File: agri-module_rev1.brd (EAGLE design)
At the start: 44 x 40 mm, 39 parts, among them M1 DMG1023, U2 PCA9570, U3 APDS-9960

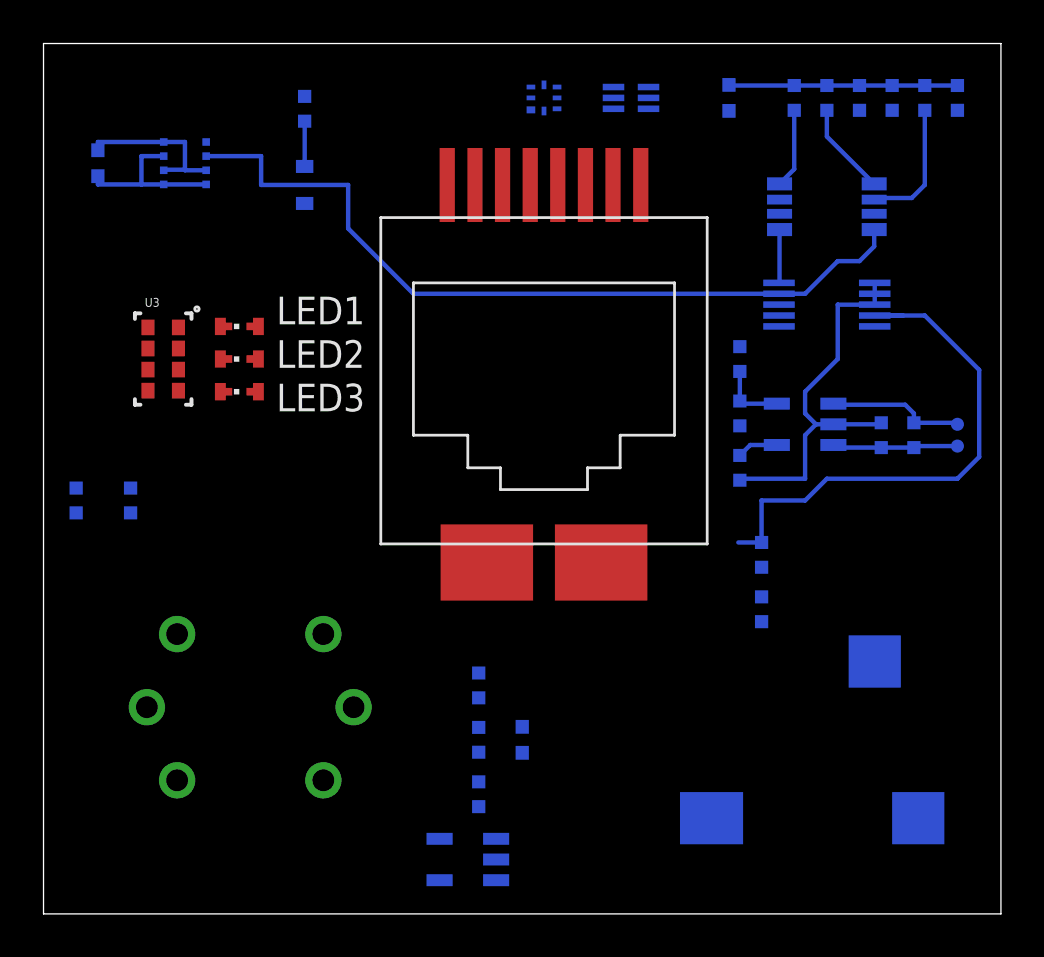
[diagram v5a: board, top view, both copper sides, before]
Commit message: Audit 1 w/ notes (wired / ready for feedback...)
______________________________________________
Schematic Feedback:
______________________________________________|
-no "zero length" junctions to parts
-add more labels, less long/jumbled connections
-tighten up the look
-replace 5v Power FET with higher power part (6601 or SIA5)
>(These are Dual N+P fets, use as darlington. Inverts signal back
aswell...)
-add very weak pull-up/downs to any fet gates. These should never be
floating
-copy michaels de-coupl caps to apds-9960
-add atleast 0R's to everything, so you dont need to cut traces
-add "lvl-trans/isolation-filter" FETs (poor mans) to i2c lines (check
Michaels schema...)
-***change i2c switch Vcc to 3.6v_HP! (otherwise, can't talk to further
boards if off)
-add RC to any power switches, so you don't get "inrush oscillation"
-add de-coupling caps and resistors to Vcc line PER PART

______________________________________________
Layout Feedback:
______________________________________________|
-add i2c addresses to board silkscreen (helps dev)
-Add mills around parts for Thermo Isolation
-tighten width of polygone pours to match trace widths (0.2032)
-Can make vias smaller (down to 0.2!)

-Use Michael's AUX jack? Or stick with mine?

______________________________________________
Feature Changes to add/design:
______________________________________________|
-See if board can be standalone and run on 5v.
>Check if all parts can use 5v & add DIP switch.
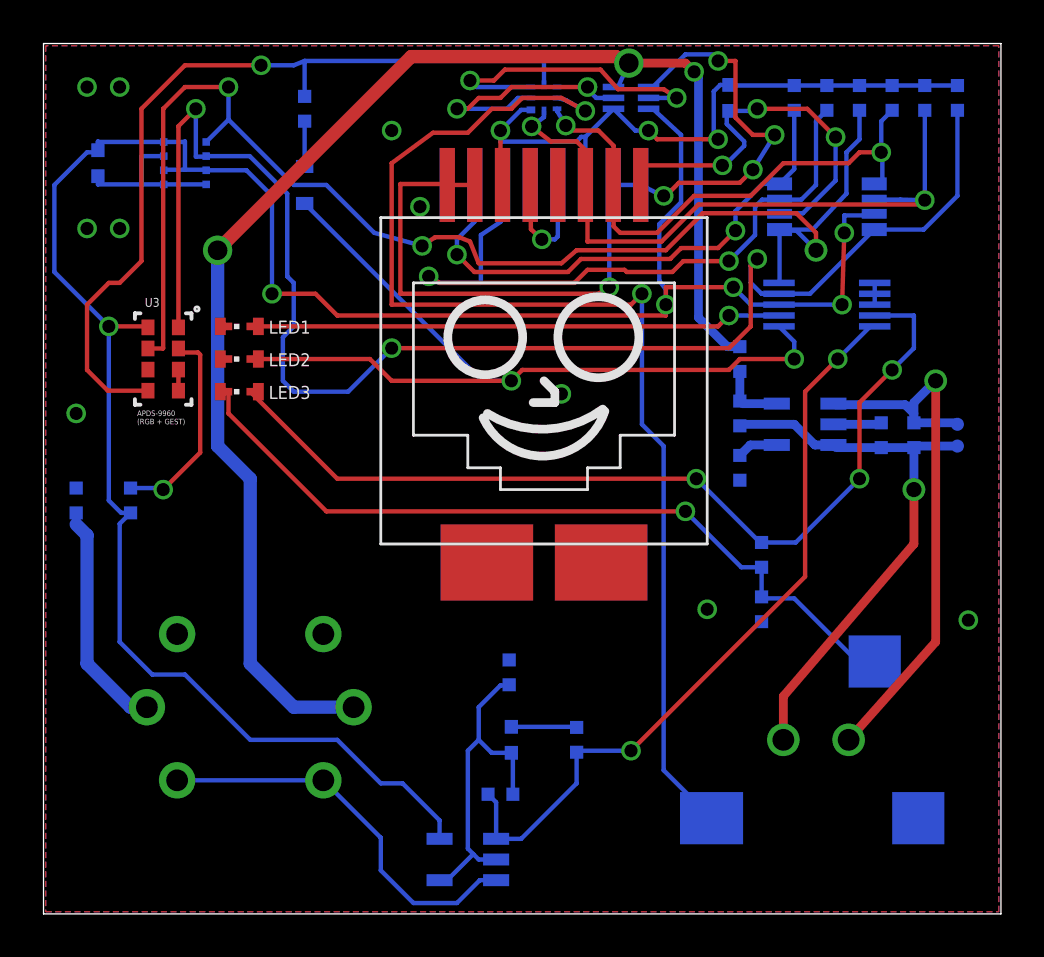
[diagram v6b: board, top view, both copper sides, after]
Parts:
- added U$9: RJ45_RA_SMD, BrainGrid - Electromechanical:RJ45_RA_SMD
- moved R18 6.00 mm to (36.0, 37.5)
- moved R3 4.50 mm to (42.0, 37.5)
- moved R7 4.50 mm to (24.5, 8.00), turned to 270 degrees
- moved R5 3.00 mm to (39.0, 37.5)
- moved R11 1.52 mm to (21.4, 11.1)
- moved R2 1.50 mm to (37.5, 37.5)
- moved R8 1.00 mm to (21.0, 5.50), turned to 0 degrees
- moved C3 0.50 mm to (21.5, 8.00), turned to 270 degrees
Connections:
- net 3.6V_HP: now also U$9.3; no longer U$5.5
- net 5V: now also U$9.1, U$9.2
- net GND: now also U$1.5, U$1.NC1, U$1.NC2, U$9.5, U$9.8, U$9.NC1, U$9.NC2; no longer U$1.7
- net N$14: now also U$1.6; no longer U$1.4
- net N$15: now also U$1.7; no longer U$1.6
- net N$7: now also U$9.6
- net N$8: now also U$9.7
- net T_SENSE: now also U$1.4, U$9.4; no longer U$1.5
- net VCC: now also U$5.5
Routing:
- net VCC: track 7.65 -> 106.5 mm, vias 0 -> 6
- net CO2_POW: track 0.00 -> 66.4 mm, vias 0 -> 3
- net N$3: track 2.46 -> 62.7 mm, vias 0 -> 3
- net EC_POW: track 0.00 -> 55.3 mm, vias 0 -> 2
- net 5V: track 0.00 -> 41.5 mm, vias 0 -> 5
- net LED_INDICATE: track 0.00 -> 40.5 mm, vias 0 -> 2
- net GEST_LED: track 0.00 -> 38.6 mm, vias 0 -> 1
- net EC_SENSE: track 0.00 -> 36.2 mm, vias 0 -> 1
- net N$16: track 0.00 -> 35.2 mm, vias 0 -> 2
- net N$11: track 36.9 -> 69.3 mm, vias 0 -> 3
- net N$7: track 0.00 -> 31.9 mm, vias 0 -> 2
- net N$14: track 6.03 -> 33.3 mm, vias 0 -> 2
- net N$5: track 0.00 -> 24.5 mm, vias 0 -> 1
- net 3.6V_HP: track 10.5 -> 31.9 mm, vias 0 -> 3
- net N$15: track 4.28 -> 25.5 mm, vias 0 -> 2
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- added copper zone on layer 1, net GND
- added copper zone on layer 16, net GND
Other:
- board text added: "( )"
- board text added: "-CO2 -CO -CH4 -CH6 -ALCOHOL -VOC -LPG -NG -O3 -H2 etc..."
- board text added: "ADS1015 (adc Mplex)"
- board text added: "APDS-9960 (RGB + GEST)"
- board text added: "BME280 (temp/press/humidity)"
- board text added: "HOT FILM points (air flow)"
- board text added: "INTERCHANGEABLE GAS SENSOR:"
- board text added: "PCA9540B (i2c board MUX)"
- board text added: "PCA9570 (gpio mux)"
- board text added: "gas sensor amp:"
- board text added: "gest -> LED2"
- board text added: "if D1 = pop, gest -> LED2"
- board text added: "if R17, bypass LED3."
- board text added: "if pop = bypass LED3, sense thru AUX if not pop = sense LED3"
- board text added: "pull-ups"

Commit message: RIPUP;
Just ripped up all lines to prepare for round 2 of layout
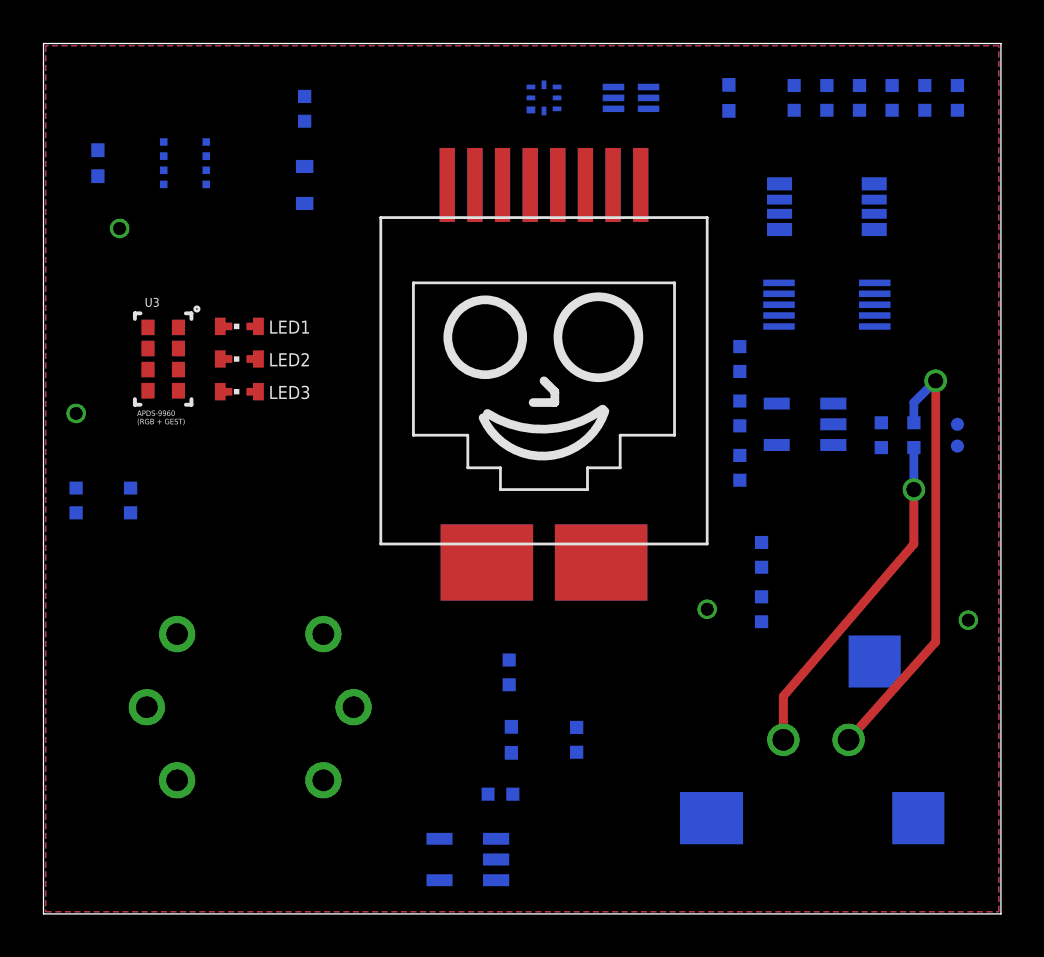
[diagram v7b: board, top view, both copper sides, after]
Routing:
- net VCC: track 106.5 -> 0.00 mm, vias 6 -> 0
- net N$11: track 69.3 -> 0.00 mm, vias 3 -> 0
- net CO2_POW: track 66.4 -> 0.00 mm, vias 3 -> 0
- net N$3: track 62.7 -> 0.00 mm, vias 3 -> 0
- net EC_POW: track 55.3 -> 0.00 mm, vias 2 -> 0
- net N$24: track 42.4 -> 0.00 mm, vias 3 -> 0
- net 5V: track 41.5 -> 0.00 mm, vias 5 -> 0
- net LED_INDICATE: track 40.5 -> 0.00 mm, vias 2 -> 0
- net GEST_LED: track 38.6 -> 0.00 mm, vias 1 -> 0
- net EC_SENSE: track 36.2 -> 0.00 mm, vias 1 -> 0
- net N$16: track 35.2 -> 0.00 mm, vias 2 -> 0
- net N$14: track 33.3 -> 0.00 mm, vias 2 -> 0
- net 3.6V_HP: track 31.9 -> 0.00 mm, vias 3 -> 0
- net N$7: track 31.9 -> 0.00 mm, vias 2 -> 0
- net GND: track 29.6 -> 0.00 mm, vias 9 -> 0
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
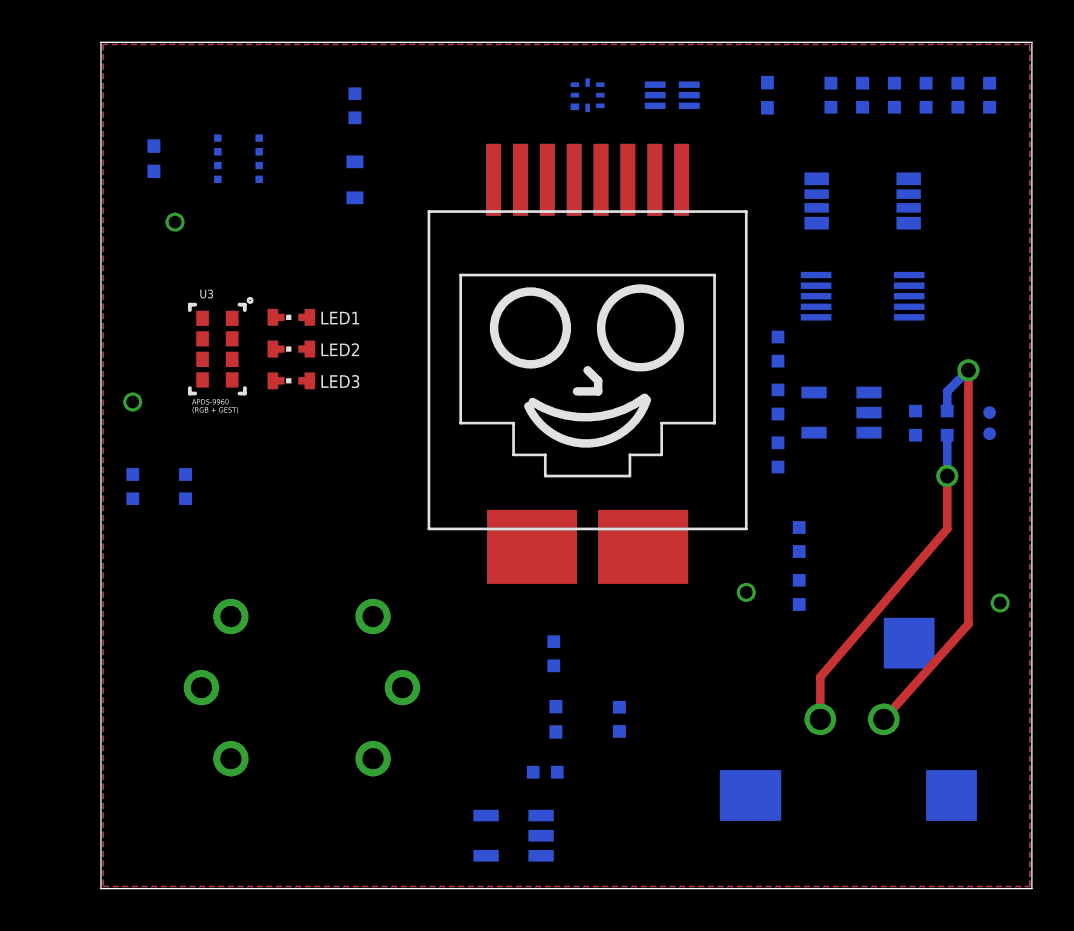
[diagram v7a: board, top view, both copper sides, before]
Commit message: fixed continuity errors
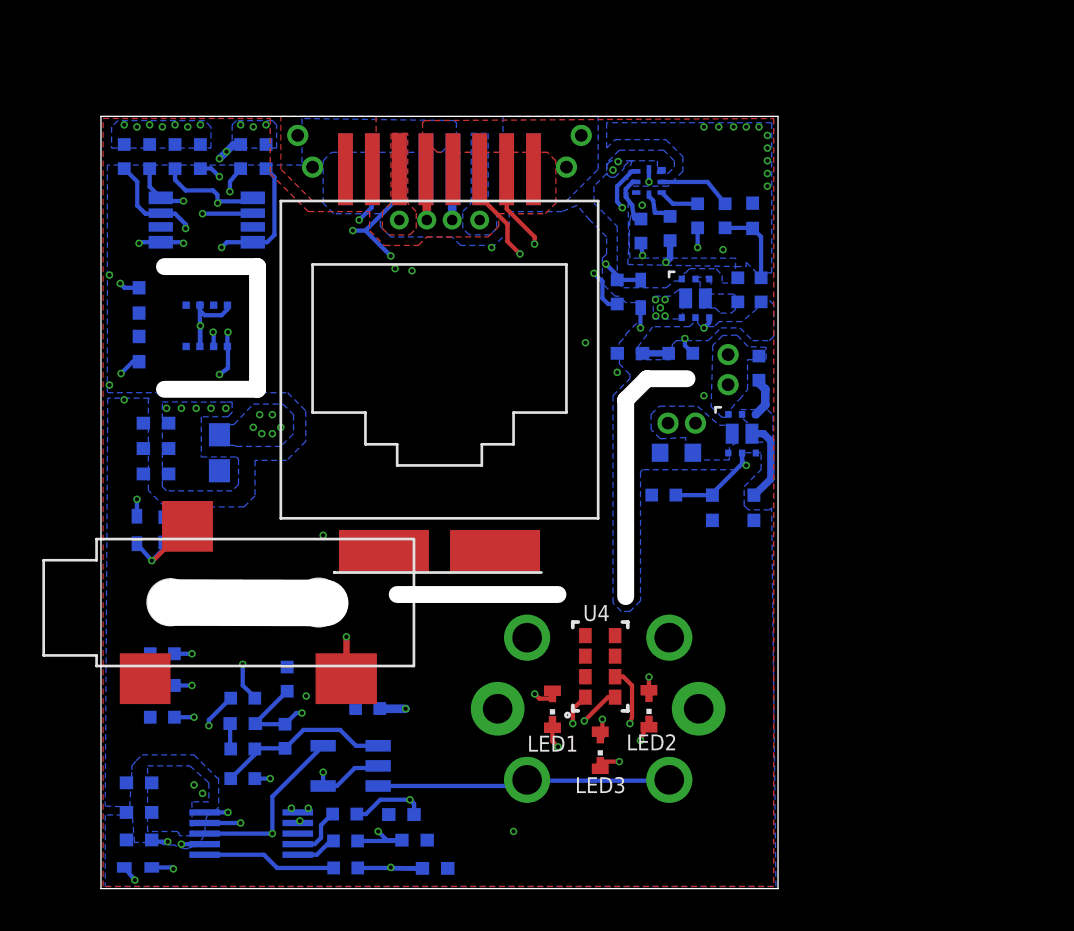
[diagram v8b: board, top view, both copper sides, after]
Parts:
- removed C1, C2: 100nF, BrainGrid - Capacitors:C0402-BG
- removed M1: DMG1023, BrainGrid - Transistors:SOT666
- removed TP3, TP4: TEST_PAD, BrainGrid - Electromechanical:TP06R
- removed U$6: PCA9540B_I2C_SWITCH, NXP:SOT505-1
- removed U$7: MG811, BrainGrid - Sensors:MG811
- removed U$8: MCP6001T, SparkFun-AnalogIC:SOT23-5
- removed U2: PCA9570, BrainGrid - MAC-PHY-Glue:XQFN8
- added C10, C11, C16, C19, C20, C5, C8: 100nF, BrainGrid - Capacitors:C0402-BG
- added C12, C13, C14, C15, C17, C4, C7, C9: 10nF, BrainGrid - Capacitors:C0402-BG
- added C18: 10uF, BrainGrid - Capacitors:C0603-BG
- added C6: 4.7uF, BrainGrid - Capacitors:C0402-BG
- added D2, D3: BAT54XV2, BrainGrid - Diodes:SOD523
- added L1: L-0603, BrainGrid - Inductors:0603
- added M2, M3: SIA527DJ, BrainGrid - Transistors:SC-70-6-L
- added R20, R21, R22, R23, R24, R26: 100R, BrainGrid - Resistors:R0402-BG
- added R25: 10R, BrainGrid - Resistors:R0402-BG
- added R27: 0R, BrainGrid - Resistors:R0402-BG
- added R28: 4.7M, BrainGrid - Resistors:R0402-BG
- added U1: PCA9570, BrainGrid - MAC-PHY-Glue:XQFN8
- added U4: APDS-9960, BrainGrid - Sensors:APDS-9960
- added U5: ADS1015, BrainGrid - Analog:ADS1015
- D1: value DB2S205 -> BAT54XV2; device EAP - Library:SSMINI2-F5-B -> BrainGrid - Diodes:SOD523
- R13: value 100R -> 1k
- R14: value 100R -> 4.7M
- R15: value 100R -> 0R
- R16, R17: value 0R -> 4.7M
- R6: value 10k -> 100R
- R8: value 5.1k -> 10k
- R9: value 100k -> 100R
- U$3: value BME280 -> MG811; device BrainGrid - Sensors:BME280 -> BrainGrid - Sensors:MG811
- U$4: value ADS1015 -> I2C_SWITCH; device BrainGrid - Analog:ADS1015 -> BrainGrid - Transistors:SOT505-1
- U3: value APDS-9960 -> BME280; device BrainGrid - Sensors:APDS-9960 -> BrainGrid - Sensors:BME280
- moved R3 39.8 mm to (2.30, 34.6)
- moved R12 37.2 mm to (2.90, 11.1), turned to 180 degrees
- moved R2 36.5 mm to (1.10, 34.6)
- moved U$2 36.1 mm to (3.29, 13.5), flipped to the top
- moved R19 33.5 mm to (11.5, 3.52), turned to 180 degrees
- moved R4 32.8 mm to (7.80, 34.6)
- moved R5 32.5 mm to (6.60, 34.6)
- moved R18 31.4 mm to (4.70, 34.6), turned to 90 degrees
- moved U$4 31.2 mm to (5.00, 31.6)
- moved R1 31.1 mm to (3.50, 34.6), turned to 90 degrees
- moved U$3 31.1 mm to (23.5, 8.50), turned to 0 degrees
- moved R15 30.9 mm to (6.70, 5.20), turned to 180 degrees
- moved R9 30.7 mm to (2.90, 8.10), turned to 180 degrees
- moved LED2 24.0 mm to (25.9, 8.50), turned to 180 degrees
- moved LED3 22.8 mm to (23.6, 6.54), turned to 180 degrees
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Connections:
- removed net CO2_POW: M1.6, R16.2, U$7.H1
- removed net EC_POW: U$2.4, U2.6
- removed net EC_SENSE: LED3.C@1, R17.1, R9.2, U$2.1
- removed net GEST_LED: R19.2, U2.4, U3.5
- removed net LED_INDICATE: D1.C, LED2.A@1, U$4.6
- removed net N$18: M1.2, U2.3
- removed net N$20: R13.2, U$8.4
- removed net N$21: R12.2, R14.2, R15.1, TP3.TP, U$8.3
- removed net N$22: R14.1, TP4.TP, U$8.1
- removed net N$23: R15.2, R16.1, U$8.5
- removed net N$24: LED3.A@1, R17.2, U$4.4
- removed net N$5 (its old number): LED1.A@1, U$4.7
- removed net N$9: U$5.3, U$7.B1, U$7.B2
- removed net T_SENSE: U$1.4, U$9.4
- new net 3.6V_HP_FILT: U$4.3
- new net ADC_LINE: C12.1, D1.C, R15.2, R22.2
- new net BRD_POW_EN: C20.1, R13.1, R26.2
- new net HEAT_EN: C19.2, M2.2, R24.2, R28.2
- new net HEAT_POW: C18.1, M2.3, M2.TAB2, U$3.H1
- new net HOST_POW_EN: C7.1, M3.2, R13.2, R17.1
- new net LED1: C15.1, LED1.A@1, R19.2
- new net LED2: C14.1, LED2.A@1, R20.2
- new net LED3: C13.1, D2.C, LED3.A@1, R21.2
- new net LED_DRIVE: D2.A, R23.2
- new net LED_DRIVING: U4.5
- new net M$65: R21.1, U5.6
- new net N$12: L1.1, M3.3, M3.TAB2
- new net N$13: R25.1, U1.4
- new net N$17: R10.2, U$3.H2
- new net N$26: M3.5, M3.6, M3.TAB1, R16.2
- new net N$66: R19.1, U5.4
- new net N$67: R20.1, U5.5
- new net N$69: R22.1, U5.7
- new net RTD: R25.2, U$2.4
- new net SCL_BRD: R5.1, U$4.5, U3.P4, U4.7, U5.10
- new net SCL_IN: R1.1, U$1.7, U$4.1, U1.7
- new net SCL_OUT: R3.1, U$4.8, U$9.7
- new net SDA_BRD: R4.1, U$4.4, U3.P3, U4.1, U5.9
- new net SDA_IN: R18.1, U$1.6, U$4.2, U1.8
- new net SDA_OUT: R2.1, U$4.7, U$9.6
- new net SPARE: D3.A, R27.1, U$1.4
- net 3.6V_HP: now also M3.4, R1.2, R16.1, R18.2, U1.1; no longer C1.1, M1.4, R1.1, R18.1, R4.2, R5.2, U2.1
- net 5V: now also M2.4, R14.1; no longer M1.1
- net GND: now also C10.2, C11.2, C12.2, C13.2, C14.2, C15.2, C16.2, C17.2, C18.2, C19.1, C20.2, C4.2, C5.2, C6.2, C7.2, C8.2, C9.2, M2.1, M3.1, R17.2, R28.1, R6.1, U$3.A1, U$3.A2, U$4.6, U1.5, U3.P1, U3.P5, U3.P7, U4.6, U5.1, U5.2, U5.3; no longer C1.2, C2.2, LED1.C@1, LED2.C@1, R13.1, U$1.NC1, U$1.NC2, U$3.P1, U$3.P5, U$3.P7, U$4.1, U$4.2, U$4.3, U$6.6, U$7.A1, U$7.A2, U$8.2, U$9.NC1, U$9.NC2, U2.5, U3.6
- net N$1: now also R26.1, U1.2; no longer M1.5, U2.2
- net N$10: now also LED2.C@1, R12.2; no longer R6.1, U3.2
- net N$11: now also LED3.C@1, R9.2; no longer R3.1, U$3.P3, U$4.9, U$6.4, U3.1
- net N$14: now also C17.1, M2.5, M2.6, M2.TAB1, R14.2; no longer R4.1, U$1.6, U$6.2, U2.8
- net N$15: now also R23.1, U1.6; no longer R5.1, U$1.7, U$6.1, U2.7
- net N$16: now also R27.2, U$9.4; no longer R7.2, R8.2, U$4.5, U$5.1
- net N$2: now also U4.3, U4.4; no longer U3.3, U3.4
- net N$3: now also C16.1, D1.A, D3.C, U$2.1; no longer R2.1, U$3.P4, U$4.10, U$6.5, U3.7
- net N$4: now also LED1.C@1, R6.2; no longer D1.A, R19.1
- net N$6: now also R24.1, U1.3; no longer R10.2, U$7.H2
- net N$7: now also U$3.B1, U$3.B2, U$5.3; no longer R18.2, U$6.7, U$9.6
- net N$8: now also R15.1, R7.2, R8.2, U$5.1; no longer R1.2, U$6.8, U$9.7
- net VCC: now also C10.1, C11.1, C4.1, C5.1, C6.1, C8.1, C9.1, L1.2, R4.2, R5.2, U3.P2, U3.P6, U3.P8, U4.8, U5.8; no longer C2.1, M1.3, R6.2, U$3.P2, U$3.P6, U$3.P8, U$4.8, U$6.3, U3.8
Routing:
- net VCC: track 0.00 -> 81.0 mm, vias 0 -> 17
- net SCL_BRD: track 0.00 -> 77.0 mm, vias 0 -> 7
- net SDA_BRD: track 0.00 -> 72.9 mm, vias 0 -> 7
- net LED_DRIVE: track 0.00 -> 66.3 mm, vias 0 -> 3
- net N$3: track 0.00 -> 37.3 mm, vias 0 -> 2
- net ADC_LINE: track 0.00 -> 36.4 mm, vias 0 -> 4
- net RTD: track 0.00 -> 35.0 mm, vias 0 -> 4
- net SCL_IN: track 0.00 -> 33.8 mm, vias 0 -> 3
- net SDA_IN: track 0.00 -> 33.1 mm, vias 0 -> 6
- net LED2: track 0.00 -> 32.2 mm, vias 0 -> 3
- net LED3: track 0.00 -> 32.2 mm, vias 0 -> 3
- net N$10: track 0.00 -> 27.8 mm, vias 0 -> 2
- net N$11: track 0.00 -> 27.7 mm, vias 0 -> 3
- net SDA_OUT: track 0.00 -> 27.0 mm, vias 0 -> 3
- net SCL_OUT: track 0.00 -> 25.5 mm, vias 0 -> 3
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- added copper zone on layer 1, net 3.6V_HP
- added copper zone on layer 16, net 3.6V_HP
- added copper zone on layer 2, net 3.6V_HP
- added copper zone on layer 1, net 5V
- added copper zone on layer 15, net 5V
- added copper zone on layer 16, net 5V
- added copper zone on layer 2, net 5V
- added copper zone on layer 15, net GND
- added copper zone on layer 16, net HEAT_POW
- added copper zone on layer 2, net HEAT_POW
- added copper zone on layer 16, net HOST_POW_EN
- added copper zone on layer 16, net N$12
- added copper zone on layer 2, net N$12
- added copper zone on layer 16, net N$14
- added copper zone on layer 16, net N$26
- added copper zone on layer 16, net VCC
- added copper zone on layer 2, net VCC
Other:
- board size 44 x 40 mm -> 32 x 36.5 mm
- board text removed: "( )"
- board text removed: "-CO2 -CO -CH4 -CH6 -ALCOHOL -VOC -LPG -NG -O3 -H2 etc..."
- board text removed: "ADS1015 (adc Mplex)"
- board text removed: "APDS-9960 (RGB + GEST)"
- board text removed: "BME280 (temp/press/humidity)"
- board text removed: "HOT FILM points (air flow)"
- board text removed: "INTERCHANGEABLE GAS SENSOR:"
- board text removed: "PCA9540B (i2c board MUX)"
- board text removed: "PCA9570 (gpio mux)"
- board text removed: "gas sensor amp:"
- board text removed: "gest -> LED2"
- board text removed: "if D1 = pop, gest -> LED2"
- board text removed: "if R17, bypass LED3."
- board text removed: "if pop = bypass LED3, sense thru AUX if not pop = sense LED3"
- board text removed: "pull-ups"
